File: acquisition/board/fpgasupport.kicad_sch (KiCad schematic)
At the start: 5 parts

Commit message: Continued initial design
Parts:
- added U6: ICE40UP5K_QFN48, symbol lattice-azonenberg:ICE40UP5K_QFN48
- gave numbers to parts that had none: 4
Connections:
- net 1V8: now also U2.F8 (VCCBATT), U2.G8 (VCCADC)
- net GND: now also U2.H7 (XADC_VREF_N), U2.H8 (XADC_VP), U2.J7 (XADC_VN), U2.J8 (XADC_VREF_P), U2.K7 (THERMAL_D_N), U2.K8 (THERMAL_D_P), U6.PAD (GND)
- net FPGA_DONE: now reaches U2.H10 (DONE)
- net FPGA_INIT_B: now reaches U2.K10 (INIT_B)
- net FPGA_RST_N: now reaches U2.L9 (PROG_B)
- new net 1V2: U6.30 (VCC), U6.5 (VCC)
- new net 2V5: U6.24 (VPP_2V5)
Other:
- note added: "TODO: Artix Decoupling TODO: ice40 decoupling"
- note removed: "TODO: Decoupling"
- company: (none) -> A. Zonenberg
- title: (none) -> Digitizer board
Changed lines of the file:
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@@
 (kicad_sch (version 20211123) (generator eeschema)
   (paper "A3")
+  (title_block
+    (title "Digitizer board")
+    (date "2022-06-22")
+    (rev "0.1")
+    (company "A. Zonenberg")
+  )
   (junction (at 163.83 127) (diameter 0) (color 0 0 0 0)
   )
@@
   )
   (junction (at 163.83 66.04) (diameter 0) (color 0 0 0 0)
+  )
+  (junction (at 76.2 171.45) (diameter 0) (color 0 0 0 0)
   )
   (junction (at 119.38 90.17) (diameter 0) (color 0 0 0 0)
@@
     (stroke (width 0) (type default) (color 0 0 0 0))
   )
+  (wire (pts (xy 76.2 171.45) (xy 76.2 173.99))
+    (stroke (width 0) (type default) (color 0 0 0 0))
+  )
   (wire (pts (xy 43.18 115.57) (xy 52.07 115.57))
     (stroke (width 0) (type default) (color 0 0 0 0))
@@
     (stroke (width 0) (type default) (color 0 0 0 0))
   )
+  (wire (pts (xy 72.39 171.45) (xy 76.2 171.45))
+    (stroke (width 0) (type default) (color 0 0 0 0))
+  )
   (wire (pts (xy 163.83 83.82) (xy 163.83 86.36))
     (stroke (width 0) (type default) (color 0 0 0 0))
@@
     (stroke (width 0) (type default) (color 0 0 0 0))
   )
-  (text "TODO: Decoupling" (at 111.76 168.91 0)
+  (text "TODO: Artix Decoupling\nTODO: ice40 decoupling" (at 111.76 168.91 0)
     (effects (font (size 1.27 1.27)) (justify left bottom))
   )
+  (label "GND" (at 52.07 95.25 180)
+    (effects (font (size 1.27 1.27)) (justify right bottom))
+  )
   (label "1V8" (at 52.07 143.51 180)
     (effects (font (size 1.27 1.27)) (justify right bottom))
   )
+  (label "GND" (at 76.2 189.23 180)
+    (effects (font (size 1.27 1.27)) (justify right bottom))
+  )
+  (label "GND" (at 52.07 92.71 180)
+    (effects (font (size 1.27 1.27)) (justify right bottom))
+  )
   (label "JTAG_TMS" (at 30.48 46.99 180)
     (effects (font (size 1.27 1.27)) (justify right bottom))
@@
   (label "JTAG_TDO" (at 35.56 115.57 180)
     (effects (font (size 1.27 1.27)) (justify right bottom))
+  )
+  (label "GND" (at 52.07 105.41 180)
+    (effects (font (size 1.27 1.27)) (justify right bottom))
+  )
+  (label "1V8" (at 163.83 24.13 0)
+    (effects (font (size 1.27 1.27)) (justify left bottom))
   )
   (label "JTAG_TDO" (at 30.48 52.07 180)
@@
     (effects (font (size 1.27 1.27)) (justify left bottom))
   )
+  (label "GND" (at 52.07 101.6 180)
+    (effects (font (size 1.27 1.27)) (justify right bottom))
+  )
+  (label "GND" (at 52.07 99.06 180)
+    (effects (font (size 1.27 1.27)) (justify right bottom))
+  )
   (label "JTAG_TCK" (at 30.48 49.53 180)
     (effects (font (size 1.27 1.27)) (justify right bottom))
@@
   (label "JTAG_TDI" (at 30.48 54.61 180)
     (effects (font (size 1.27 1.27)) (justify right bottom))
+  )
+  (label "GND" (at 52.07 107.95 180)
+    (effects (font (size 1.27 1.27)) (justify right bottom))
+  )
+  (label "1V8" (at 163.83 29.21 0)
+    (effects (font (size 1.27 1.27)) (justify left bottom))
   )
   (label "GND" (at 52.07 146.05 180)
@@
     (effects (font (size 1.27 1.27)) (justify left))
   )
+  (hierarchical_label "FPGA_INIT_B" (shape bidirectional) (at 52.07 133.35 180)
+    (effects (font (size 1.27 1.27)) (justify right))
+  )
   (hierarchical_label "1V8" (shape input) (at 30.48 29.21 180)
     (effects (font (size 1.27 1.27)) (justify right))
@@
     (effects (font (size 1.27 1.27)) (justify right))
   )
+  (hierarchical_label "FPGA_RST_N" (shape input) (at 52.07 135.89 180)
+    (effects (font (size 1.27 1.27)) (justify right))
+  )
+  (hierarchical_label "FPGA_DONE" (shape output) (at 52.07 130.81 180)
+    (effects (font (size 1.27 1.27)) (justify right))
+  )
+  (hierarchical_label "3V3" (shape input) (at 111.76 181.61 180)
+    (effects (font (size 1.27 1.27)) (justify right))
+  )
   (hierarchical_label "GND" (shape input) (at 30.48 31.75 180)
+    (effects (font (size 1.27 1.27)) (justify right))
+  )
+  (hierarchical_label "2V5" (shape input) (at 76.2 184.15 180)
+    (effects (font (size 1.27 1.27)) (justify right))
+  )
+  (hierarchical_label "1V2" (shape input) (at 72.39 171.45 180)
     (effects (font (size 1.27 1.27)) (justify right))
   )
   (symbol (lib_id "xilinx-azonenberg:XILINX_JTAG") (at 30.48 57.15 0) (unit 1)
     (in_bom yes) (on_board yes)
-    (property "Reference" "J?" (id 0) (at 39.37 59.69 0)
+    (property "Reference" "J1" (id 0) (at 39.37 59.69 0)
       (effects (font (size 1.524 1.524)) (justify left))
     )
@@
   (symbol (lib_id "device:R") (at 48.26 125.73 90) (unit 1)
     (in_bom yes) (on_board yes)
-    (property "Reference" "R?" (id 0) (at 48.26 123.19 90))
+    (property "Reference" "R3" (id 0) (at 48.26 123.19 90))
     (property "Value" "33" (id 1) (at 48.26 125.73 90))
     (property "Footprint" "" (id 2) (at 48.26 127.508 90)
@@
   (symbol (lib_id "xilinx-azonenberg:XC7AxT-xFTG256x") (at 57.15 148.59 0) (unit 1)
     (in_bom yes) (on_board yes)
-    (property "Reference" "U?" (id 0) (at 57.15 151.661 0)
+    (property "Reference" "U2" (id 0) (at 57.15 151.661 0)
       (effects (font (size 1.524 1.524)) (justify left))
     )
@@
     (pin "N8")
   )
+  (symbol (lib_id "lattice-azonenberg:ICE40UP5K_QFN48") (at 80.01 190.5 0) (unit 4)
+    (in_bom yes) (on_board yes)
+    (property "Reference" "U6" (id 0) (at 80.01 191.5349 0)
+      (effects (font (size 1.27 1.27)) (justify left))
+    )
+    (property "Value" "ICE40UP5K_QFN48" (id 1) (at 80.01 194.31 0)
+      (effects (font (size 1.27 1.27)) (justify left))
+    )
+    (property "Footprint" "" (id 2) (at 80.01 190.5 0)
+      (effects (font (size 1.27 1.27)) hide)
+    )
+    (property "Datasheet" "" (id 3) (at 80.01 190.5 0)
+      (effects (font (size 1.27 1.27)) hide)
+    )
+    (pin "1")
+    (pin "22")
+    (pin "24")
+    (pin "29")
+    (pin "30")
+    (pin "33")
+    (pin "5")
+    (pin "PAD")
+  )
   (symbol (lib_id "xilinx-azonenberg:XC7AxT-xFTG256x") (at 124.46 148.59 0) (unit 2)
     (in_bom yes) (on_board yes)
-    (property "Reference" "U?" (id 0) (at 124.46 151.661 0)
+    (property "Reference" "U2" (id 0) (at 124.46 151.661 0)
       (effects (font (size 1.524 1.524)) (justify left))
     )
@@
   (symbol (lib_id "device:R") (at 39.37 115.57 90) (unit 1)
     (in_bom yes) (on_board yes)
-    (property "Reference" "R?" (id 0) (at 39.37 113.03 90))
+    (property "Reference" "R2" (id 0) (at 39.37 113.03 90))
     (property "Value" "33" (id 1) (at 39.37 115.57 90))
     (property "Footprint" "" (id 2) (at 39.37 117.348 90)

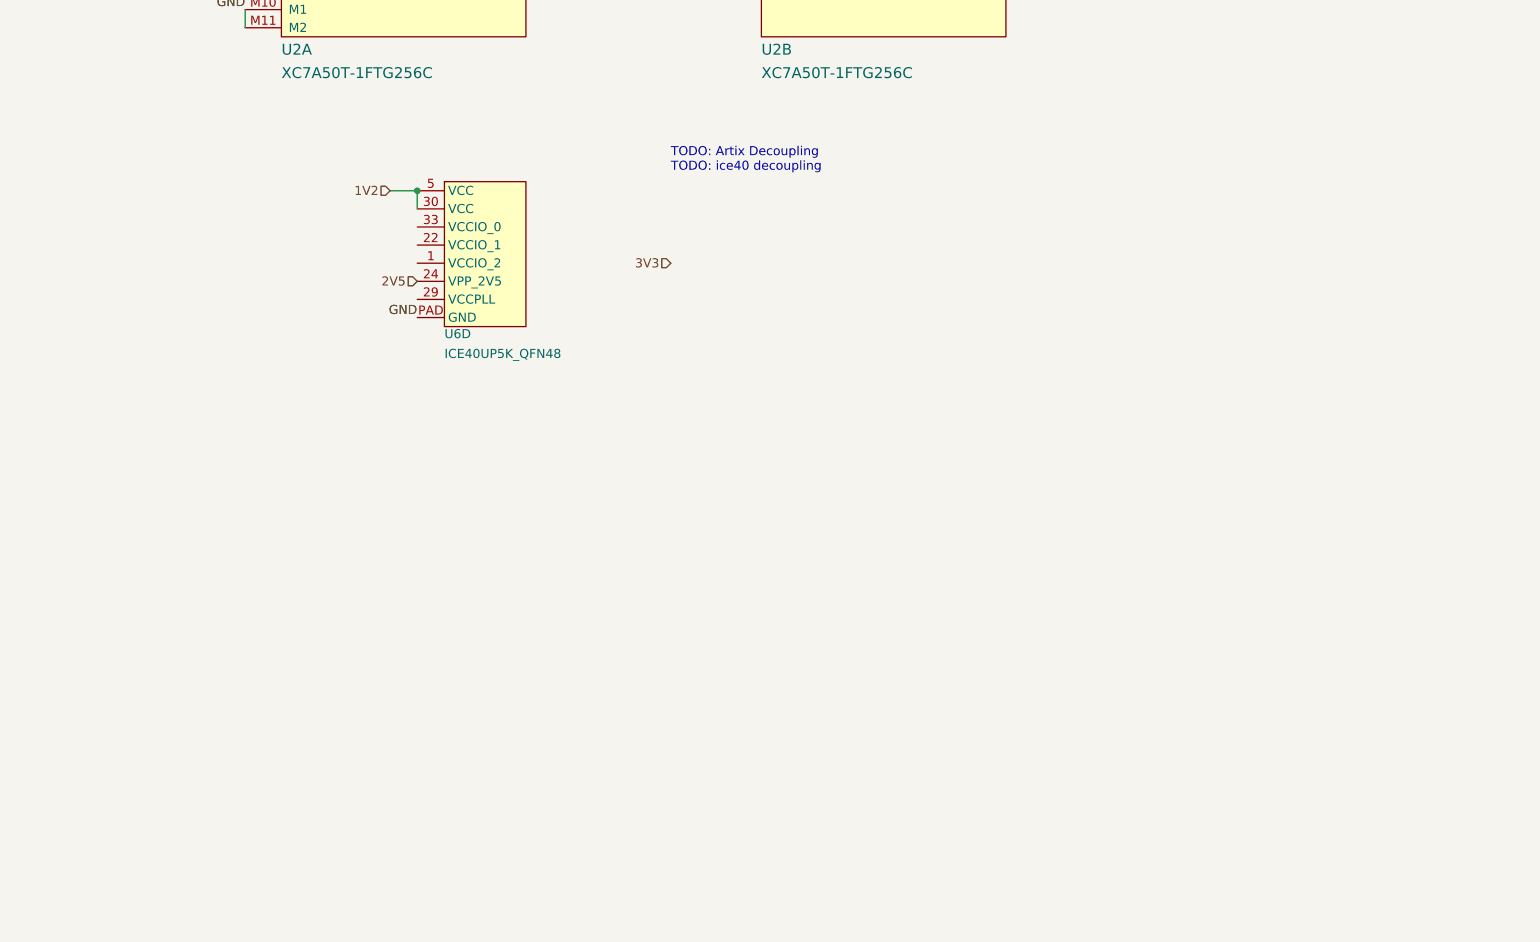
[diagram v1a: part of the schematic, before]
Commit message: Updated schematic with a lot of level shifting and support stuff, power decoupling, etc. Almost done except power supply and protection diodes
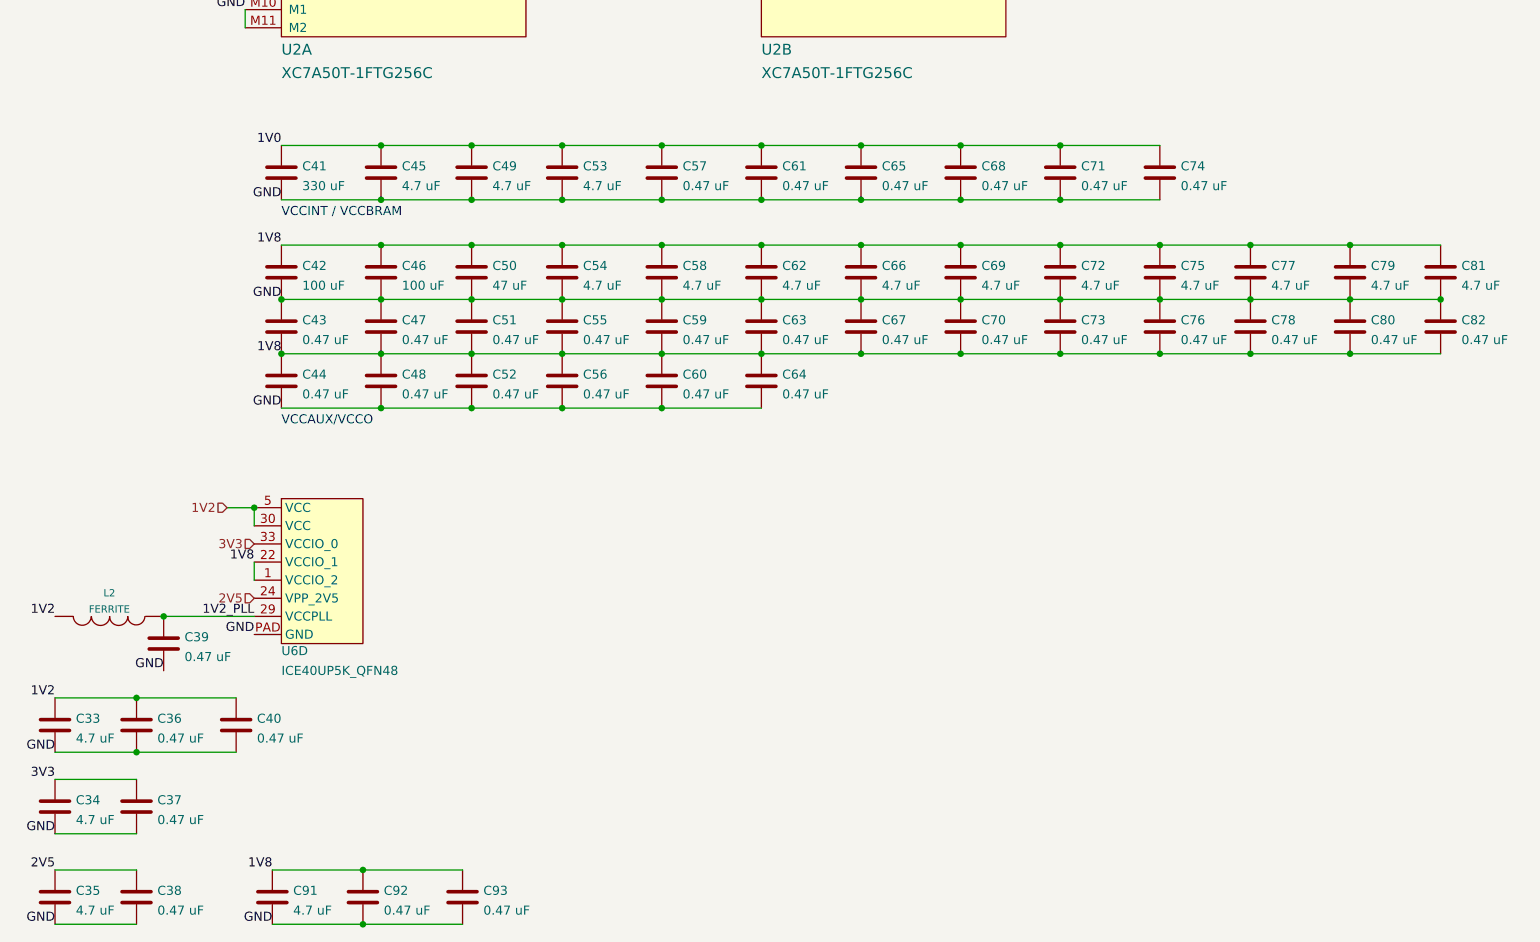
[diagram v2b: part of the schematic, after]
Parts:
- added C33, C34, C35, C45, C49, C53, C54, C58, C62, C66, C69, C72, C75, C77, C79, C81, C91: 4.7 uF, symbol device:C
- added C36, C37, C38, C39, C40, C43, C44, C47, C48, C51, C52, C55, C56, C57, C59, C60, C61, C63, C64, C65, C67, C68, C70, C71, C73, C74, C76, C78, C80, C82, C92, C93: 0.47 uF, symbol device:C
- added C41: 330 uF, symbol device:C
- added C42, C46: 100 uF, symbol device:C
- added C50: 47 uF, symbol device:C
- added L2: FERRITE, symbol passive-azonenberg:INDUCTOR_PWROUT
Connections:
- net 1V0: now also C41.1, C45.1, C49.1, C53.1, C57.1, C61.1, C65.1, C68.1, C71.1, C74.1
- net 1V2: now also C33.1, C36.1, C40.1, L2.2
- net 1V8: now also U6.1 (VCCIO_2), U6.22 (VCCIO_1), C42.1, C43.2, C44.1, C46.1, C47.2, C48.1, C50.1, C51.2, C52.1, C54.1, C55.2, C56.1, C58.1, C59.2, C60.1, C62.1, C63.2, C64.1, C66.1, C67.2, C69.1, C70.2, C72.1, C73.2, C75.1, C76.2, C77.1, C78.2, C79.1, C80.2, C81.1, C82.2, C91.1, C92.1, C93.1
- net 2V5: now also C35.1, C38.1
- net 3V3: now also U6.33 (VCCIO_0), C34.1, C37.1
- net GND: now also C33.2, C34.2, C35.2, C36.2, C37.2, C38.2, C39.2, C40.2, C41.2, C42.2, C43.1, C44.2, C45.2, C46.2, C47.1, C48.2, C49.2, C50.2, C51.1, C52.2, C53.2, C54.2, C55.1, C56.2, C57.2, C58.2, C59.1, C60.2, C61.2, C62.2, C63.1, C64.2, C65.2, C66.2, C67.1, C68.2, C69.2, C70.1, C71.2, C72.2, C73.1, C74.2, C75.2, C76.1, C77.2, C78.1, C79.2, C80.1, C81.2, C82.1, C91.2, C92.2, C93.2
- net 1V2_PLL: now reaches U6.29 (VCCPLL)
- net 1V2_PLL: now also C39.1, L2.1
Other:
- note added: "VCCAUX/VCCO"
- note added: "VCCINT / VCCBRAM"
- note removed: "TODO: Artix Decoupling TODO: ice40 decoupling"
- moved on the sheet: U6D

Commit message: Lots of progress on power supply design, added a bunch of test points, etc
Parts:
- added TP4, TP5, TP6: TESTPOINT, symbol conn:CONN_01X01
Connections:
- net FPGA_DONE: now also TP4.1 (P1), TP6.1 (P1)
- net FPGA_INIT_B: now also TP5.1 (P1)
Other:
- note added: "JTAG program/debug header for main FPGA 1.8V logic levels Standard Xilinx pinout"
- note added: "Test points for main FPGA boot status/control pins"
- moved on the sheet: J1
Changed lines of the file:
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@@
   (title_block
     (title "Digitizer board")
-    (date "2022-07-04")
+    (date "2022-07-05")
     (rev "0.1")
     (company "A. Zonenberg")
@@
   (junction (at 36.83 250.19) (diameter 0) (color 0 0 0 0)
   )
-  (junction (at 30.48 34.29) (diameter 0) (color 0 0 0 0)
+  (junction (at 205.74 34.29) (diameter 0) (color 0 0 0 0)
   )
   (junction (at 163.83 38.1) (diameter 0) (color 0 0 0 0)
@@
   (junction (at 152.4 172.72) (diameter 0) (color 0 0 0 0)
   )
-  (junction (at 30.48 39.37) (diameter 0) (color 0 0 0 0)
+  (junction (at 205.74 39.37) (diameter 0) (color 0 0 0 0)
   )
   (junction (at 71.12 172.72) (diameter 0) (color 0 0 0 0)
@@
   (junction (at 119.38 46.99) (diameter 0) (color 0 0 0 0)
   )
-  (junction (at 30.48 36.83) (diameter 0) (color 0 0 0 0)
+  (junction (at 205.74 36.83) (diameter 0) (color 0 0 0 0)
   )
   (junction (at 110.49 194.31) (diameter 0) (color 0 0 0 0)
@@
   (junction (at 110.49 186.69) (diameter 0) (color 0 0 0 0)
   )
-  (no_connect (at 30.48 44.45))
-  (no_connect (at 30.48 57.15))
+  (no_connect (at 205.74 44.45))
+  (no_connect (at 205.74 57.15))
   (wire (pts (xy 25.4 254) (xy 36.83 254))
     (stroke (width 0) (type default) (color 0 0 0 0))
@@
     (stroke (width 0) (type default) (color 0 0 0 0))
   )
-  (wire (pts (xy 30.48 39.37) (xy 30.48 41.91))
+  (wire (pts (xy 205.74 39.37) (xy 205.74 41.91))
     (stroke (width 0) (type default) (color 0 0 0 0))
   )
@@
     (stroke (width 0) (type default) (color 0 0 0 0))
   )
-  (wire (pts (xy 30.48 31.75) (xy 30.48 34.29))
+  (wire (pts (xy 205.74 31.75) (xy 205.74 34.29))
     (stroke (width 0) (type default) (color 0 0 0 0))
   )
@@
     (stroke (width 0) (type default) (color 0 0 0 0))
   )
-  (wire (pts (xy 30.48 34.29) (xy 30.48 36.83))
+  (wire (pts (xy 205.74 34.29) (xy 205.74 36.83))
     (stroke (width 0) (type default) (color 0 0 0 0))
   )
@@
     (stroke (width 0) (type default) (color 0 0 0 0))
   )
-  (wire (pts (xy 30.48 36.83) (xy 30.48 39.37))
+  (wire (pts (xy 205.74 36.83) (xy 205.74 39.37))
     (stroke (width 0) (type default) (color 0 0 0 0))
   )
@@
   (wire (pts (xy 57.15 165.1) (xy 71.12 165.1))
     (stroke (width 0) (type default) (color 0 0 0 0))
+  )
+  (text "JTAG program/debug header for main FPGA\n1.8V logic levels\nStandard Xilinx pinout"
+    (at 213.36 71.12 0)
+    (effects (font (size 1.27 1.27)) (justify left bottom))
+  )
+  (text "Test points for main FPGA boot status/control pins"
+    (at 207.01 152.4 0)
+    (effects (font (size 1.27 1.27)) (justify left bottom))
   )
   (text "VCCINT / VCCBRAM" (at 57.15 175.26 0)
@@
     (effects (font (size 1.27 1.27)) (justify right bottom))
   )
+  (label "FPGA_DONE" (at 213.36 129.54 0)
+    (effects (font (size 1.27 1.27)) (justify left bottom))
+  )
   (label "1V8" (at 52.07 143.51 180)
     (effects (font (size 1.27 1.27)) (justify right bottom))
@@
     (effects (font (size 1.27 1.27)) (justify right bottom))
   )
-  (label "JTAG_TMS" (at 30.48 46.99 180)
+  (label "FPGA_DONE" (at 213.36 148.59 0)
+    (effects (font (size 1.27 1.27)) (justify left bottom))
+  )
+  (label "JTAG_TMS" (at 205.74 46.99 180)
     (effects (font (size 1.27 1.27)) (justify right bottom))
   )
@@
     (effects (font (size 1.27 1.27)) (justify right bottom))
   )
-  (label "JTAG_TDO" (at 30.48 52.07 180)
+  (label "JTAG_TDO" (at 205.74 52.07 180)
     (effects (font (size 1.27 1.27)) (justify right bottom))
   )
@@
     (effects (font (size 1.27 1.27)) (justify right bottom))
   )
-  (label "JTAG_TCK" (at 30.48 49.53 180)
+  (label "FPGA_INIT_B" (at 213.36 139.7 0)
+    (effects (font (size 1.27 1.27)) (justify left bottom))
+  )
+  (label "JTAG_TCK" (at 205.74 49.53 180)
     (effects (font (size 1.27 1.27)) (justify right bottom))
   )
@@
     (effects (font (size 1.27 1.27)) (justify right bottom))
   )
-  (label "JTAG_TDI" (at 30.48 54.61 180)
+  (label "JTAG_TDI" (at 205.74 54.61 180)
     (effects (font (size 1.27 1.27)) (justify right bottom))
   )
@@
     (effects (font (size 1.27 1.27)) (justify right))
   )
-  (hierarchical_label "1V8" (shape input) (at 30.48 29.21 180)
+  (hierarchical_label "1V8" (shape input) (at 205.74 29.21 180)
     (effects (font (size 1.27 1.27)) (justify right))
   )
@@
     (effects (font (size 1.27 1.27)) (justify right))
   )
-  (hierarchical_label "GND" (shape input) (at 30.48 31.75 180)
+  (hierarchical_label "GND" (shape input) (at 205.74 31.75 180)
     (effects (font (size 1.27 1.27)) (justify right))
   )
@@
     (pin "2")
   )
+  (symbol (lib_id "conn:CONN_01X01") (at 208.28 148.59 180) (unit 1)
+    (in_bom yes) (on_board yes) (fields_autoplaced)
+    (property "Reference" "TP6" (id 0) (at 208.28 143.4805 0))
+    (property "Value" "TESTPOINT" (id 1) (at 208.28 146.2556 0))
+    (property "Footprint" "" (id 2) (at 208.28 148.59 0)
+      (effects (font (size 1.27 1.27)) hide)
+    )
+    (property "Datasheet" "" (id 3) (at 208.28 148.59 0)
+      (effects (font (size 1.27 1.27)) hide)
+    )
+    (pin "1")
+  )
   (symbol (lib_id "device:C") (at 36.83 257.81 0) (unit 1)
     (in_bom yes) (on_board yes) (fields_autoplaced)
@@
     (pin "2")
   )
-  (symbol (lib_id "xilinx-azonenberg:XILINX_JTAG") (at 30.48 57.15 0) (unit 1)
+  (symbol (lib_id "xilinx-azonenberg:XILINX_JTAG") (at 205.74 57.15 0) (unit 1)
     (in_bom yes) (on_board yes)
-    (property "Reference" "J1" (id 0) (at 39.37 59.69 0)
+    (property "Reference" "J1" (id 0) (at 214.63 59.69 0)
       (effects (font (size 1.524 1.524)) (justify left))
     )
-    (property "Value" "XILINX_JTAG" (id 1) (at 39.37 62.969 0)
+    (property "Value" "XILINX_JTAG" (id 1) (at 214.63 62.969 0)
       (effects (font (size 1.524 1.524)) (justify left))
     )
-    (property "Footprint" "" (id 2) (at 30.48 57.15 0)
+    (property "Footprint" "" (id 2) (at 205.74 57.15 0)
       (effects (font (size 1.524 1.524)))
     )
-    (property "Datasheet" "" (id 3) (at 30.48 57.15 0)
+    (property "Datasheet" "" (id 3) (at 205.74 57.15 0)
       (effects (font (size 1.524 1.524)))
     )
@@
     (pin "1")
     (pin "2")
+  )
+  (symbol (lib_id "conn:CONN_01X01") (at 208.28 139.7 180) (unit 1)
+    (in_bom yes) (on_board yes) (fields_autoplaced)
+    (property "Reference" "TP5" (id 0) (at 208.28 134.5905 0))
+    (property "Value" "TESTPOINT" (id 1) (at 208.28 137.3656 0))
+    (property "Footprint" "" (id 2) (at 208.28 139.7 0)
+      (effects (font (size 1.27 1.27)) hide)
+    )
+    (property "Datasheet" "" (id 3) (at 208.28 139.7 0)
+      (effects (font (size 1.27 1.27)) hide)
+    )
+    (pin "1")
   )
   (symbol (lib_id "device:C") (at 57.15 190.5 0) (unit 1)
@@
     (pin "2")
   )
+  (symbol (lib_id "conn:CONN_01X01") (at 208.28 129.54 180) (unit 1)
+    (in_bom yes) (on_board yes) (fields_autoplaced)
+    (property "Reference" "TP4" (id 0) (at 208.28 124.4305 0))
+    (property "Value" "TESTPOINT" (id 1) (at 208.28 127.2056 0))
+    (property "Footprint" "" (id 2) (at 208.28 129.54 0)
+      (effects (font (size 1.27 1.27)) hide)
+    )
+    (property "Datasheet" "" (id 3) (at 208.28 129.54 0)
+      (effects (font (size 1.27 1.27)) hide)
+    )
+    (pin "1")
+  )
   (symbol (lib_id "device:C") (at 166.37 190.5 0) (unit 1)

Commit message: More power supply work, added PLL loop filter, soft start, began assigning footprints
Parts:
- C33, C34, C35, C45, C49, C53, C54, C58, C62, C66, C69, C72, C75, C77, C79, C81, C91: footprint (none) -> azonenberg_pcb:EIA_0603_CAP_NOSILK
- C36, C37, C38, C39, C40, C43, C44, C47, C48, C51, C52, C55, C56, C57, C59, C60, C61, C63, C64, C65, C67, C68, C70, C71, C73, C74, C76, C78, C80, C82, C92, C93: footprint (none) -> azonenberg_pcb:EIA_0402_CAP_NOSILK
- J1: footprint (none) -> azonenberg_pcb:XILINX_JTAG_PTH_MOLEX_0878311420
- R2, R3: footprint (none) -> azonenberg_pcb:EIA_0402_RES_NOSILK
- TP4, TP5, TP6: footprint (none) -> azonenberg_pcb:TESTPOINT_SMT_0.5MM
- U2: footprint (none) -> azonenberg_pcb:BGA_256_17x17_FULLARRAY_1MM_0.4MM_FTG256
